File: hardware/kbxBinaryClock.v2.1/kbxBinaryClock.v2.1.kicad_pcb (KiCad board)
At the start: 2 copper layers, 127 x 114.3 mm, 136 parts, among them J1 Jack-DC, J2 Conn_01x06, J3 Conn_02x03_Odd_Even, P1 STM32_SWD_USART, Q1 2N7002, Q10 Q_NPN_BCE, Q11 Q_NPN_BCE, Q2 2N7002, Q3 2N7002, Q4 2N7002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

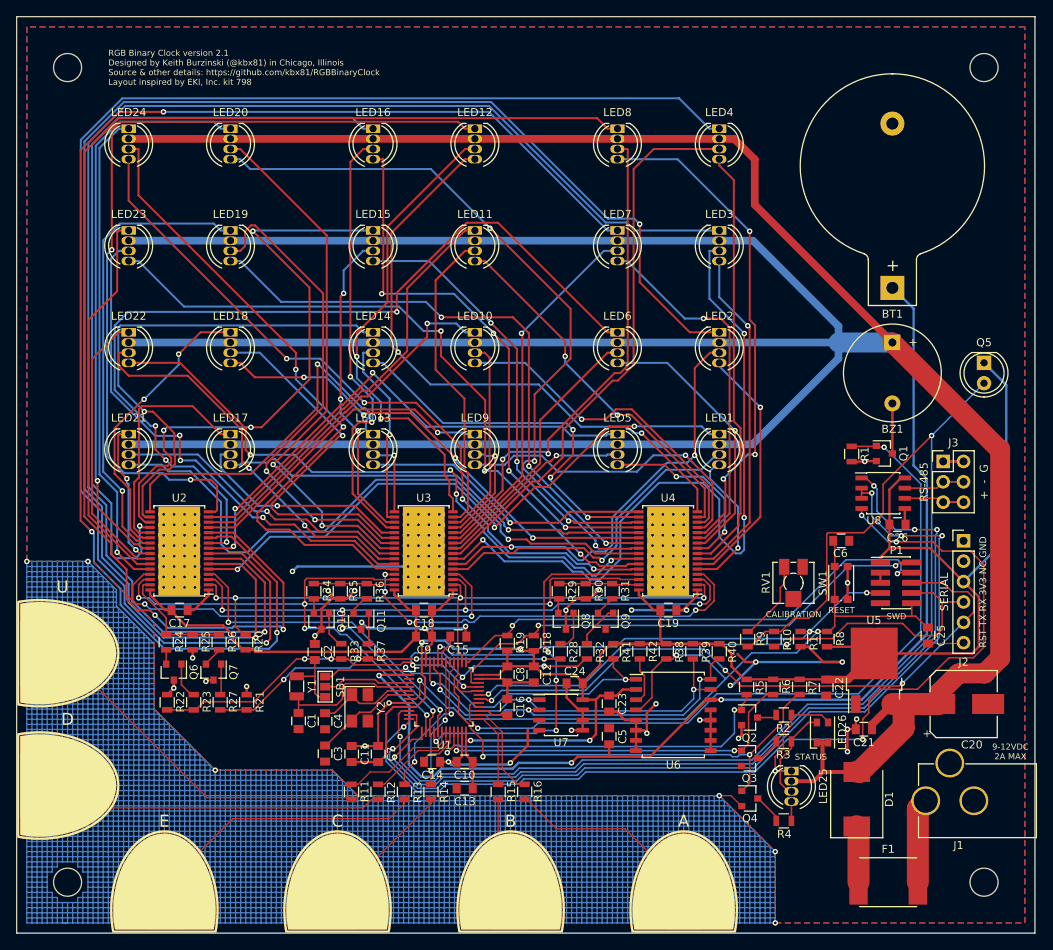
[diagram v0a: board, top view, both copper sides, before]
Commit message: Modified PCBs to accommodate a 16mm buzzer element
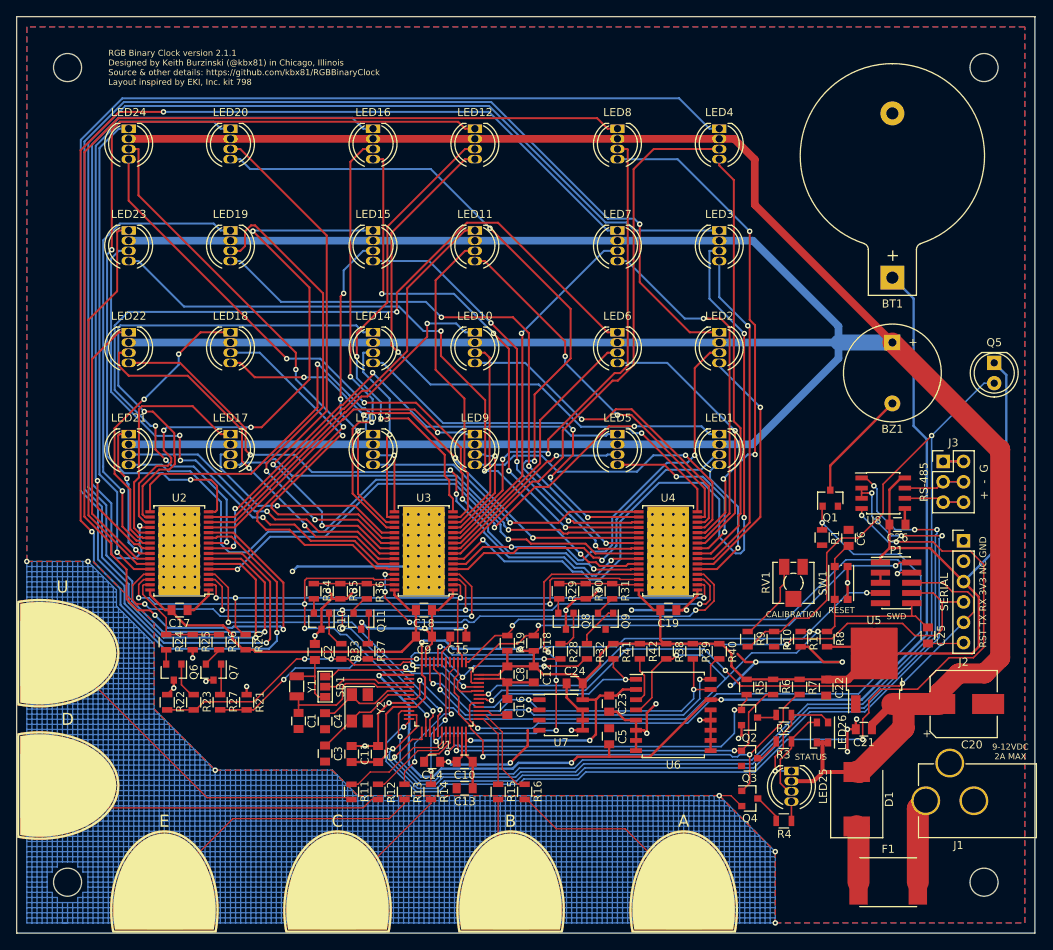
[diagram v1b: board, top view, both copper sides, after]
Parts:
- moved R1 11.1 mm to (194.4, 98.0)
- moved Q1 8.75 mm to (195.5, 93.1), turned to 90 degrees
- moved Q5 1.27 mm to (215.9, 76.2)
- moved BT1 1.27 mm to (203.2, 65.6)
- moved C6 0.99 mm to (197.7, 98.0), turned to 270 degrees
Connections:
- RV1 pad 3: (no net) -> GND
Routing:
- net Net-(BZ1-Pad2): track 5.61 -> 14.0 mm
- net BEEP: track 93.8 -> 89.8 mm
- net GND: track 6538.3 -> 6535.1 mm, vias 38 -> 37
- net +BATT: track 135.6 -> 136.9 mm
- net +3V3: track 279.1 -> 278.5 mm
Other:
- board text added: "RGB Binary Clock version 2.1.1 Designed by Keith Burzinski (@kbx81) in Chicago, Illinois Source & other details: https://github.com/kbx81/RGBBinaryClock Layout inspired by EKI, Inc. kit 798"
- board text removed: "RGB Binary Clock version 2.1 Designed by Keith Burzinski (@kbx81) in Chicago, Illinois Source & other details: https://github.com/kbx81/RGBBinaryClock Layout inspired by EKI, Inc. kit 798"

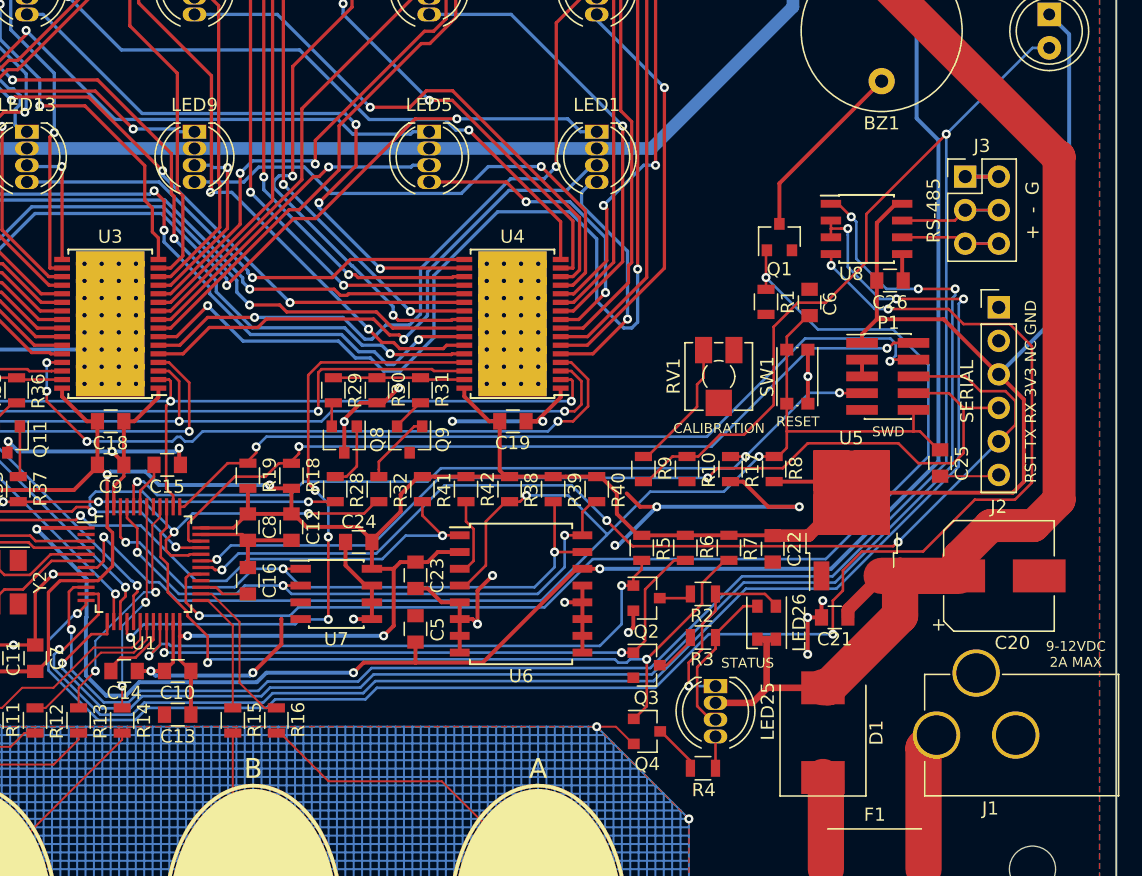
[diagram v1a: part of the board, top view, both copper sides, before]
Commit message: Added BoM, hw README, PCB tweaks
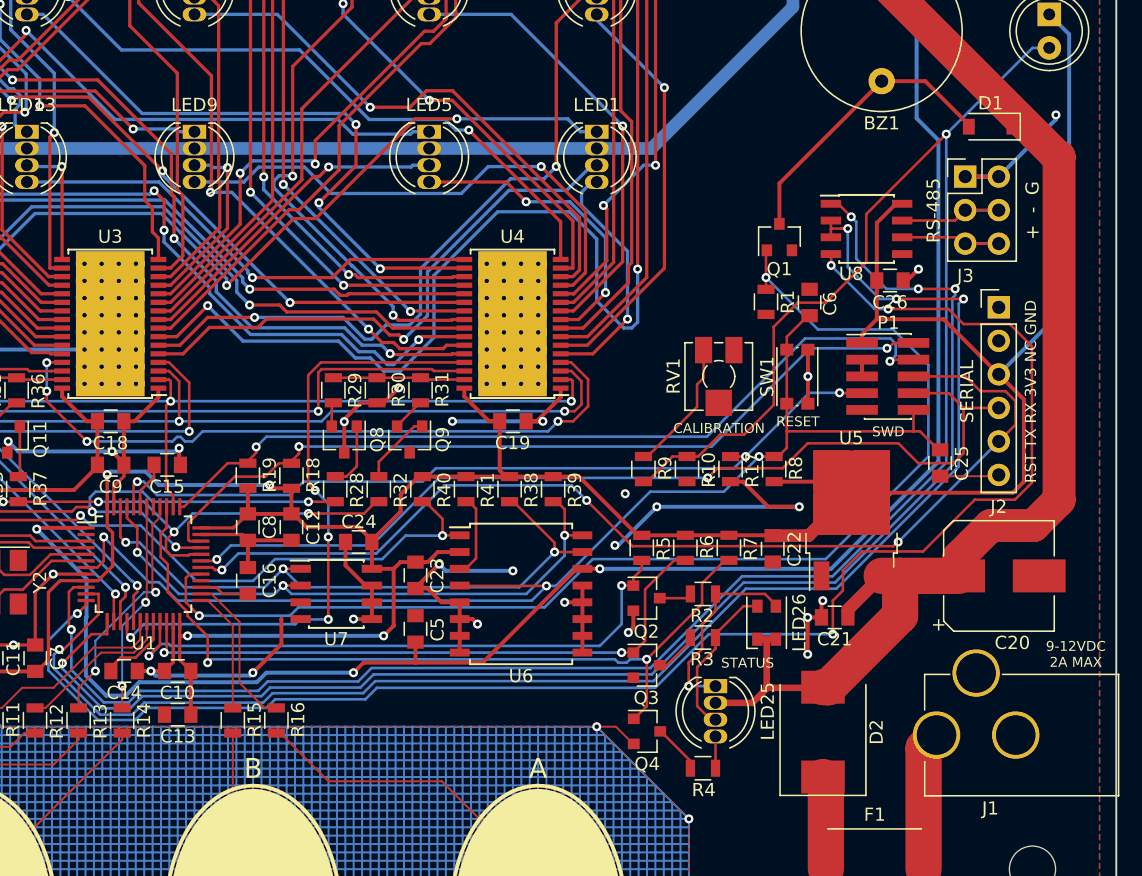
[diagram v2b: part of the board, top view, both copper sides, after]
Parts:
- removed R42: 10K, Resistors_SMD:R_0805
- added D2: S3A, Diodes_SMD:D_SMC, F.Cu at (198.8, 130.6)
- D1: value S3A -> 1N4148; footprint Diodes_SMD:D_SMC -> Diodes_SMD:D_SOD-123
- R38: value 10K -> 3K3
- R40: value 3K3 -> 10K
- moved D1 47.6 mm to (211.5, 84.7), turned to 180 degrees
- moved R40 13.2 mm to (168.4, 112.2)
- moved R41 3.30 mm to (171.7, 112.2)
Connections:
- D1 pad 1: Net-(D1-Pad1) -> +9V
- D1 pad 2: +9V -> Net-(BZ1-Pad2)
- F1 pad 1: Net-(D1-Pad1) -> Net-(D2-Pad1)
- J2 pad 2: (no net) -> Net-(J2-Pad2)
- P1 pad 9: (no net) -> Net-(P1-Pad9)
- R38 pad 2: /MCU/RESET -> /MCU/I2C1_SDA
- R39 pad 2: /MCU/I2C1_SDA -> /MCU/I2C1_SCL
- R40 pad 2: /MCU/I2C1_SCL -> /MCU/OSC32_IN
- R41 pad 2: /MCU/OSC32_IN -> Net-(R41-Pad2)
- U1 pad 2: (no net) -> Net-(U1-Pad2)
- U1 pad 28: (no net) -> Net-(U1-Pad28)
- U1 pad 41: (no net) -> Net-(U1-Pad41)
- U6 pad 3: Net-(R42-Pad2) -> Net-(R41-Pad2)
- U7 pad 3: (no net) -> Net-(U7-Pad3)
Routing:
- net /MCU/RESET: track 103.8 -> 93.1 mm
- net Net-(BZ1-Pad2): track 14.0 -> 22.1 mm
- net GND: track 6535.1 -> 6542.6 mm, vias 37 -> 40
- net Net-(D1-Pad1): track 7.21 -> 0.00 mm
- net Net-(D2-Pad1): track 0.00 -> 7.08 mm
- net Net-(R41-Pad2): track 0.00 -> 6.31 mm
- net Net-(R42-Pad2): track 6.02 -> 0.00 mm
- net +9V: track 485.0 -> 489.5 mm
- net +3V3: track 278.5 -> 277.2 mm
- net /MCU/I2C1_SDA: track 47.0 -> 47.9 mm
- net /MCU/I2C1_SCL: track 47.1 -> 46.5 mm
- net (no net): vias 0 -> 1

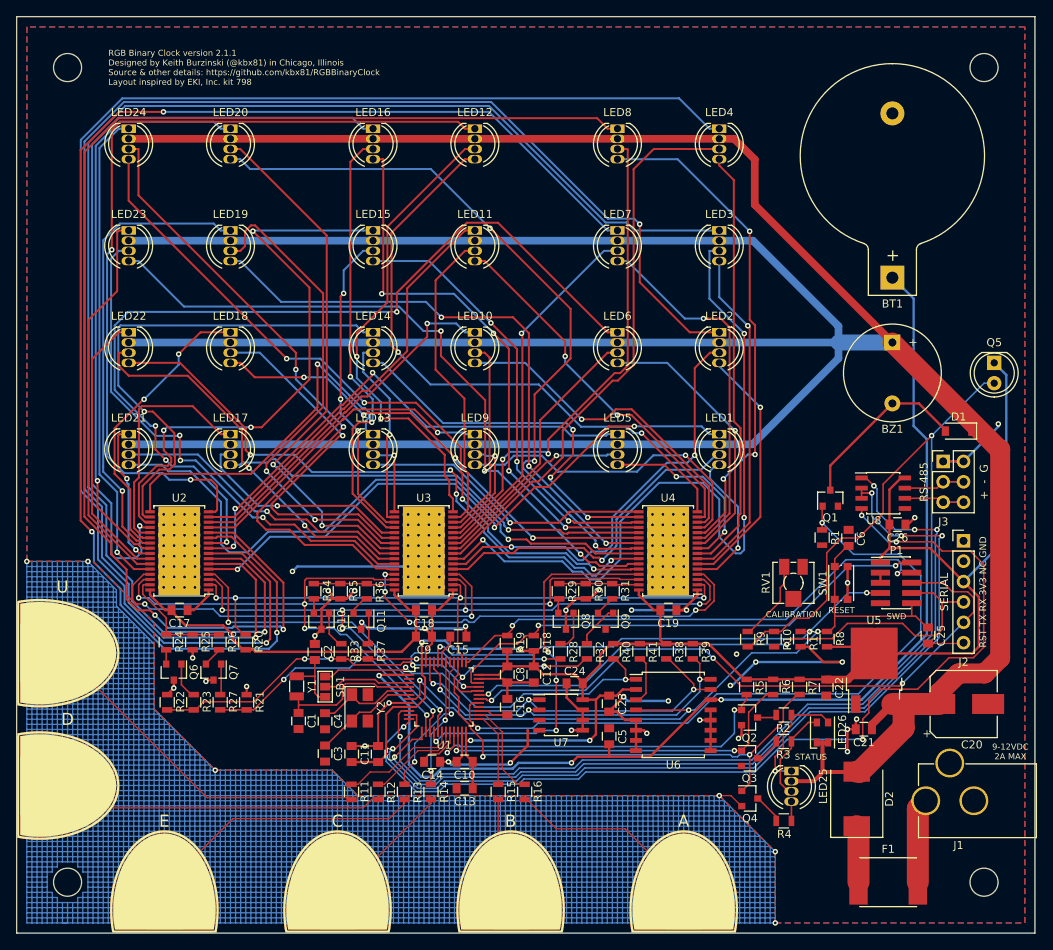
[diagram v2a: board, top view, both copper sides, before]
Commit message: Added disconnect on DS323x reset line
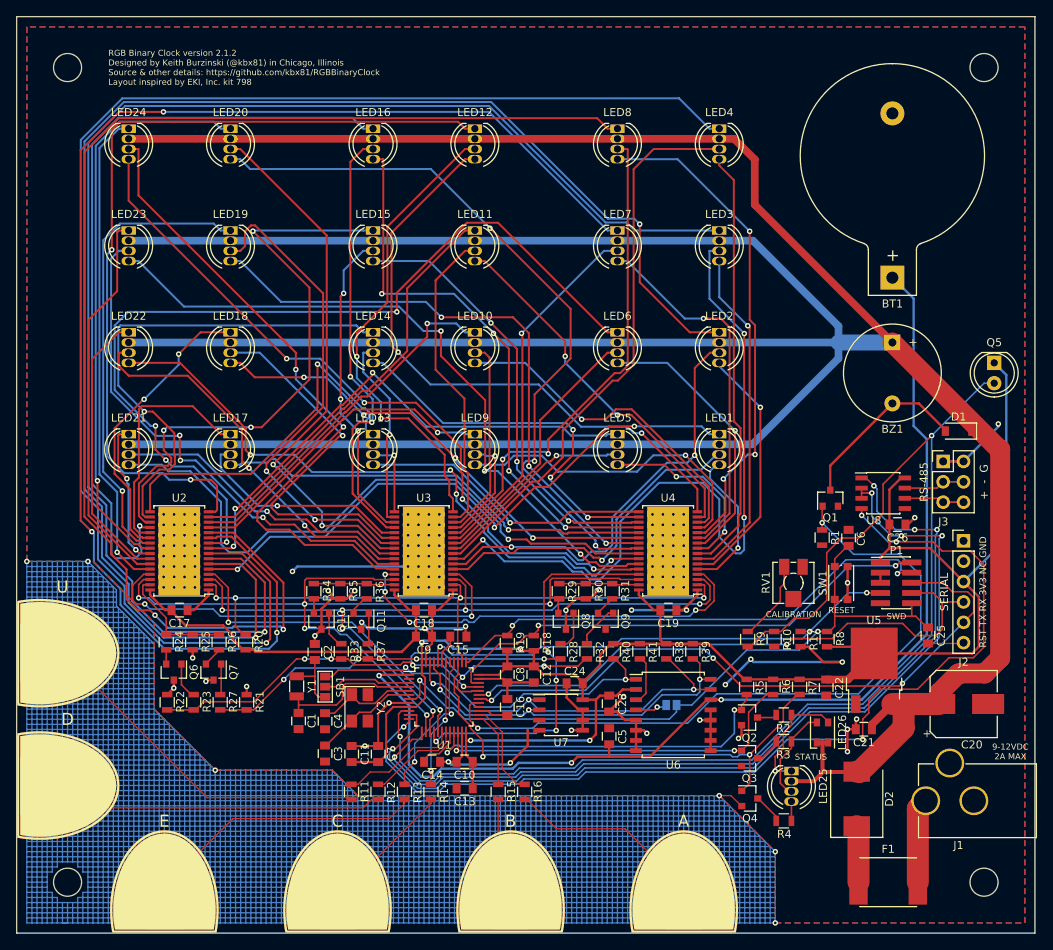
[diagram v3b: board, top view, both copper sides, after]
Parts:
- added SB2: GS2, Connectors:GS2, B.Cu at (175.6, 118.9)
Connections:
- U6 pad 4: /MCU/RESET -> Net-(SB2-Pad2)
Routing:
- net /MCU/RESET: track 93.1 -> 87.1 mm, vias 3 -> 2
- net GND: track 6542.6 -> 6537.7 mm, vias 40 -> 39
- net Net-(SB2-Pad2): track 0.00 -> 4.06 mm, vias 0 -> 1
- net (no net): vias 1 -> 0
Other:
- board text added: "RGB Binary Clock version 2.1.2 Designed by Keith Burzinski (@kbx81) in Chicago, Illinois Source & other details: https://github.com/kbx81/RGBBinaryClock Layout inspired by EKI, Inc. kit 798"
- board text removed: "RGB Binary Clock version 2.1.1 Designed by Keith Burzinski (@kbx81) in Chicago, Illinois Source & other details: https://github.com/kbx81/RGBBinaryClock Layout inspired by EKI, Inc. kit 798"
